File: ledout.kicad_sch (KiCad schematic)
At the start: 0 parts

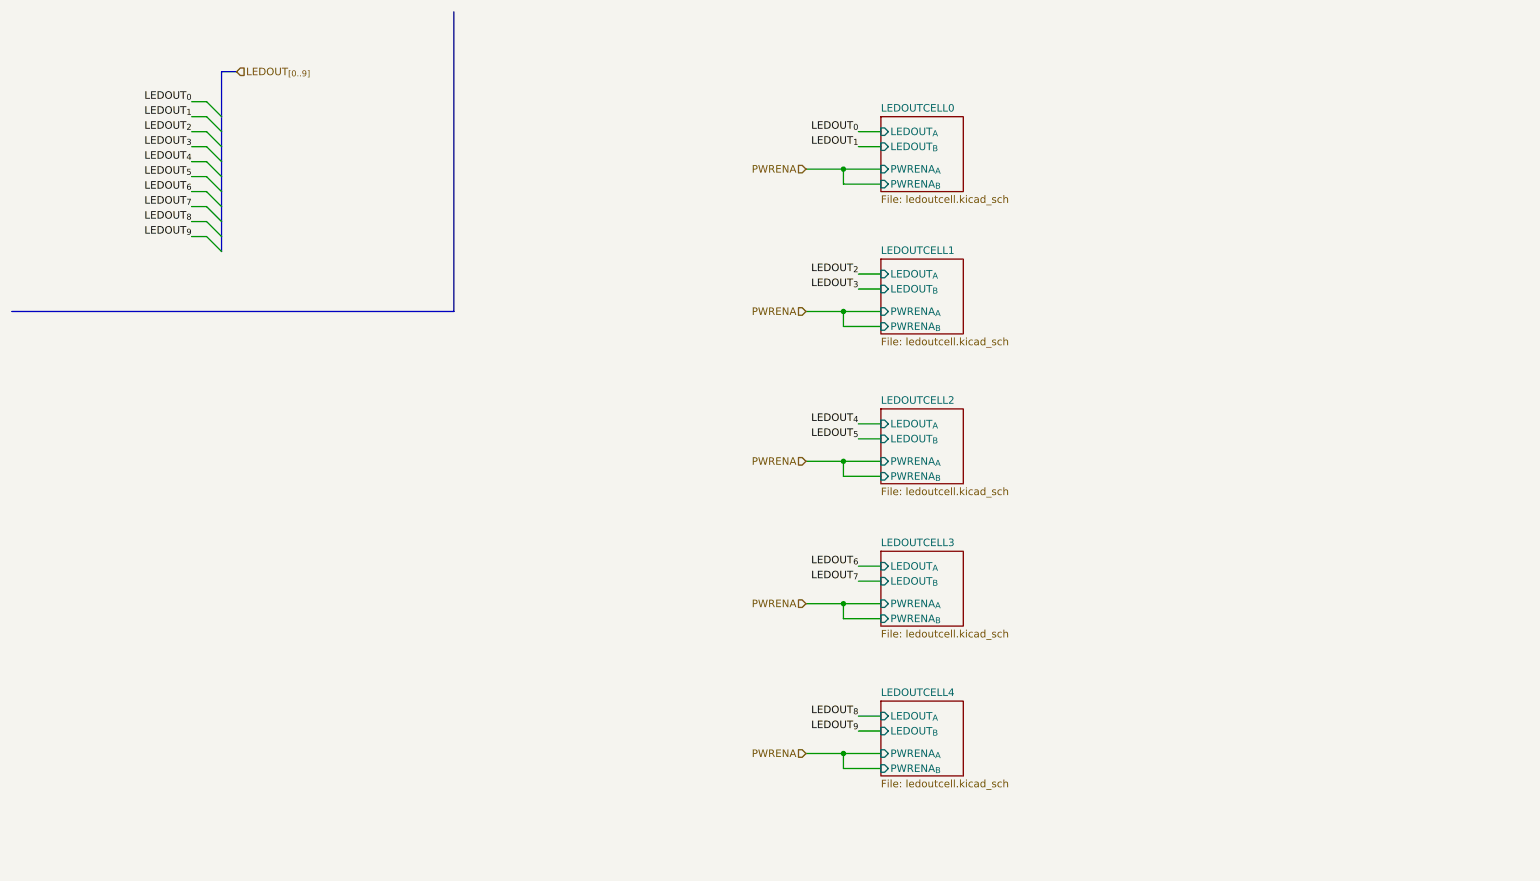
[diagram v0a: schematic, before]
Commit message: Added Testpoints
Schematic and PCB updated
Also probably some other smaller changes that I forgot about
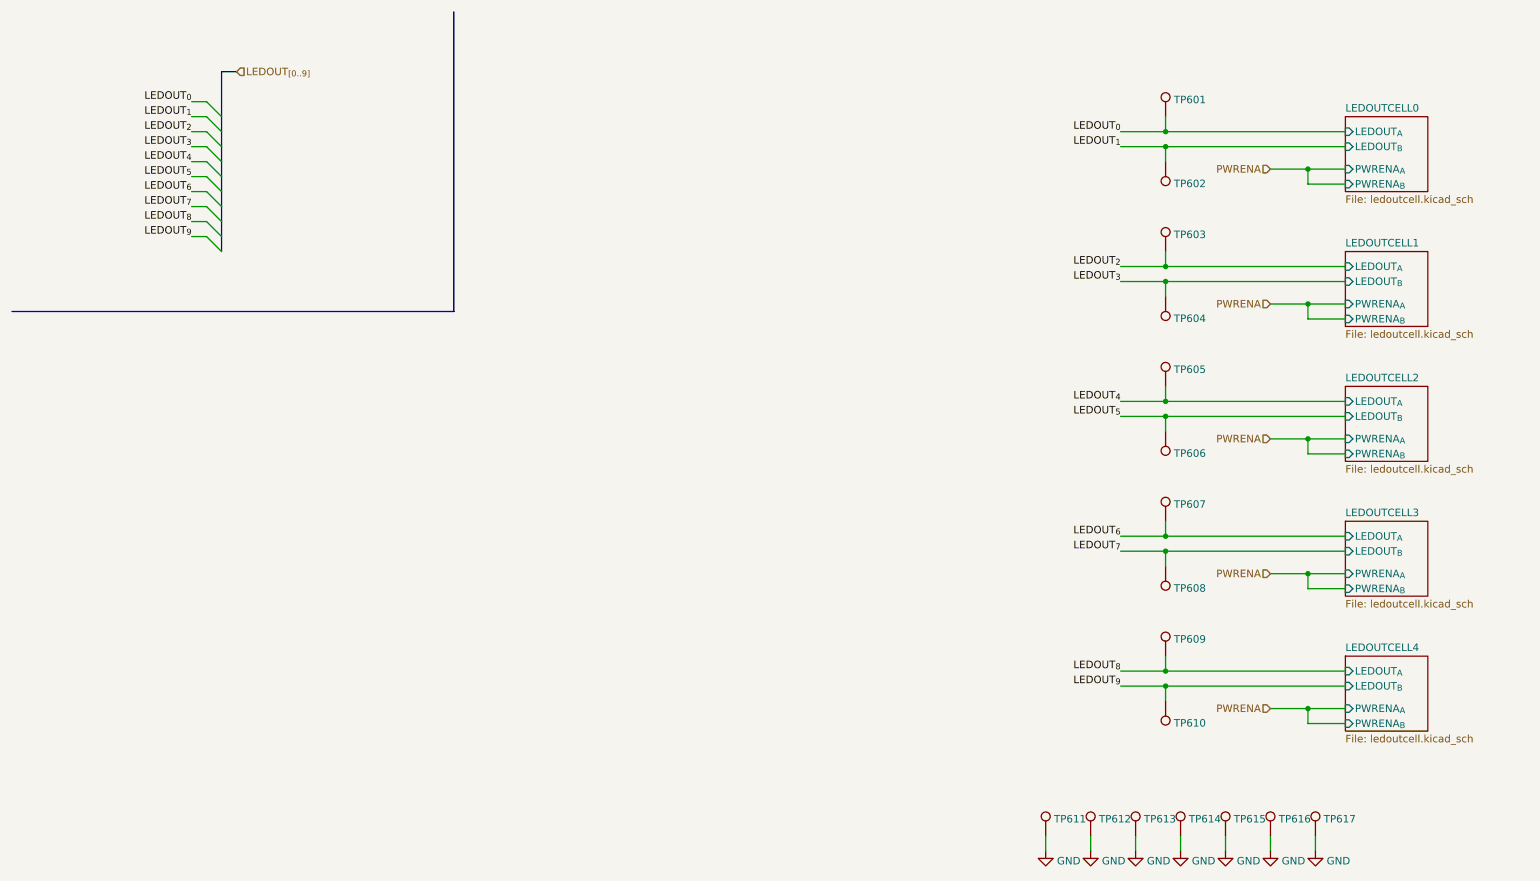
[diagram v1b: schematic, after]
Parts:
- added TP601, TP602, TP603, TP604, TP605, TP606, TP607, TP608, TP609, TP610, TP611, TP612, TP613, TP614, TP615, TP616, TP617: TestPoint, TestPoint:TestPoint_Loop_D1.80mm_Drill1.0mm_Beaded, symbol Connector:TestPoint
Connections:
- net LEDOUT_{0}: now also TP601.1
- net LEDOUT_{1}: now also TP602.1
- net LEDOUT_{2}: now also TP603.1
- net LEDOUT_{3}: now also TP604.1
- net LEDOUT_{4}: now also TP605.1
- net LEDOUT_{5}: now also TP606.1
- net LEDOUT_{6}: now also TP607.1
- net LEDOUT_{7}: now also TP608.1
- net LEDOUT_{8}: now also TP609.1
- net LEDOUT_{9}: now also TP610.1
- new net GND: TP611.1, TP612.1, TP613.1, TP614.1, TP615.1, TP616.1, TP617.1
